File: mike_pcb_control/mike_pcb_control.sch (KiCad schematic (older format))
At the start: 5 parts, among them J1 Conn_01x06_Male, J4 Raspberry_Pi_2_3, U3 LLC-4channel, U4 Adafruit_Feather_Pinout

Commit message: Updating the design files
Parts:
- added C1: C, Capacitor_THT:C_Radial_D8.0mm_H7.0mm_P3.50mm, symbol Device:C
- added J2: Conn_01x06_Male, Connector_PinHeader_2.54mm:PinHeader_1x06_P2.54mm_Vertical, symbol Connector:Conn_01x06_Male
- added J3, J5: Conn_01x03_Male, Connector_PinHeader_2.54mm:PinHeader_1x03_P2.54mm_Vertical, symbol Connector:Conn_01x03_Male
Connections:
- net +5V: now also C1.1, J2.5 (Pin_5), J2.6 (Pin_6), J3.3 (Pin_3), J5.3 (Pin_3)
- net GND: now also C1.2, J2.3 (Pin_3), J2.4 (Pin_4), J3.2 (Pin_2), J5.2 (Pin_2)
- net RX5V: now also J2.1 (Pin_1)
- net SCL3V3: now also U4.18
- net SCL5V: now also A2.24 (A5)
- net SDA3V3: now also U4.17
- net SDA5V: now also A2.23 (A4)
- net TX5V: now also J2.2 (Pin_2)
- net A0: now reaches A2.19 (A0)
- net A0: now also J5.1 (Pin_1)
- net A1: now reaches A2.20 (A1)
- net A1: now also J3.1 (Pin_1)
- removed net SCL_IMU: A2.24 (A5), U4.18
- removed net SDA_IMU: A2.23 (A4), U4.17
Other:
- moved on the sheet: J1, U3

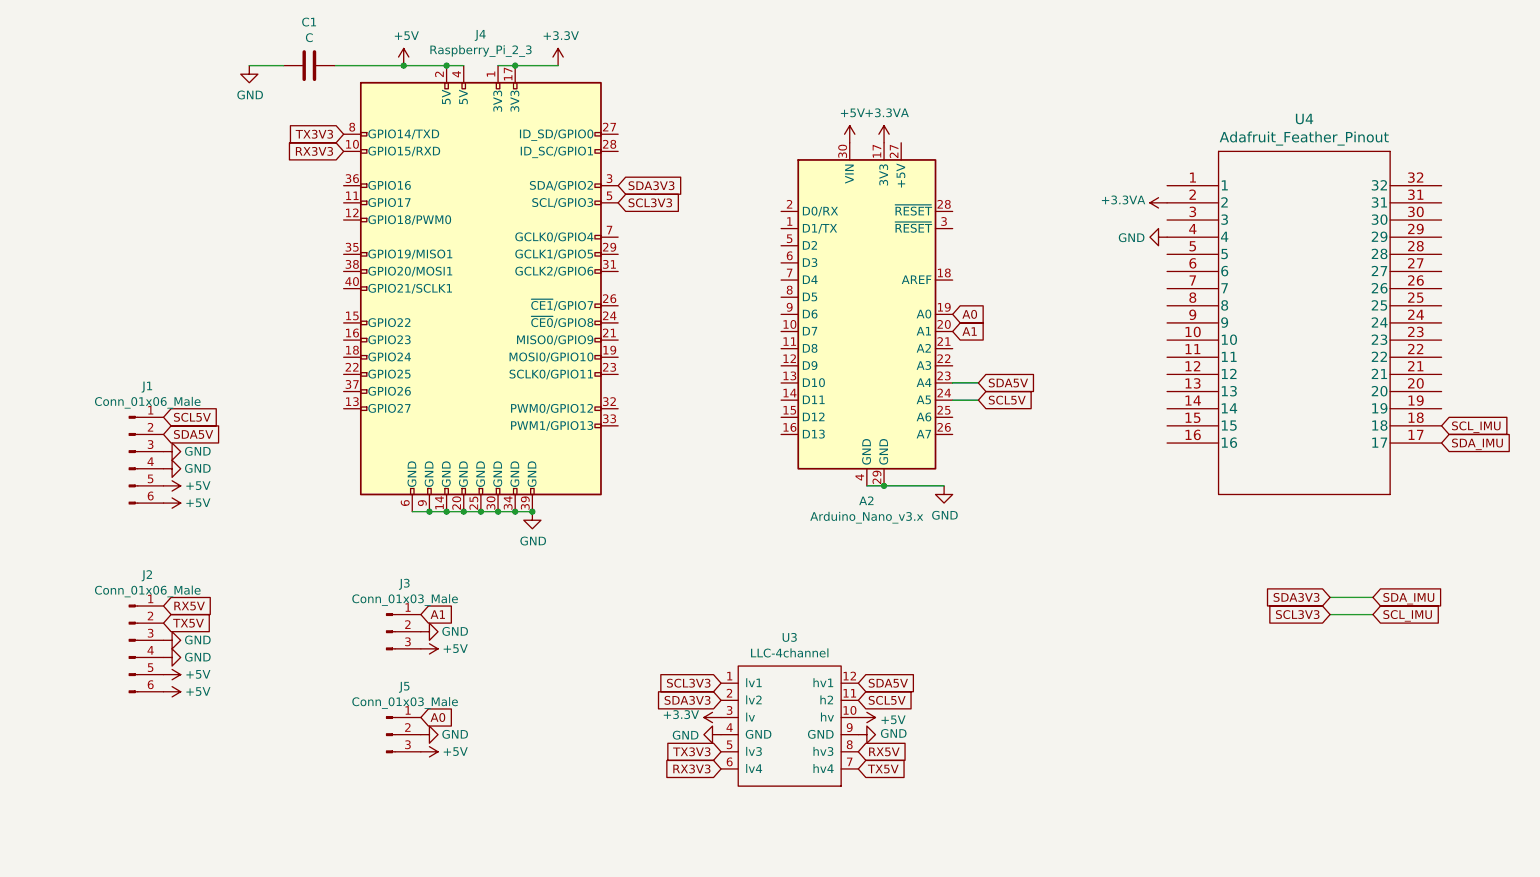
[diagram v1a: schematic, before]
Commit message: PCB bugfix, I2C seperated
I2C for IMU seperated from main I2C bus
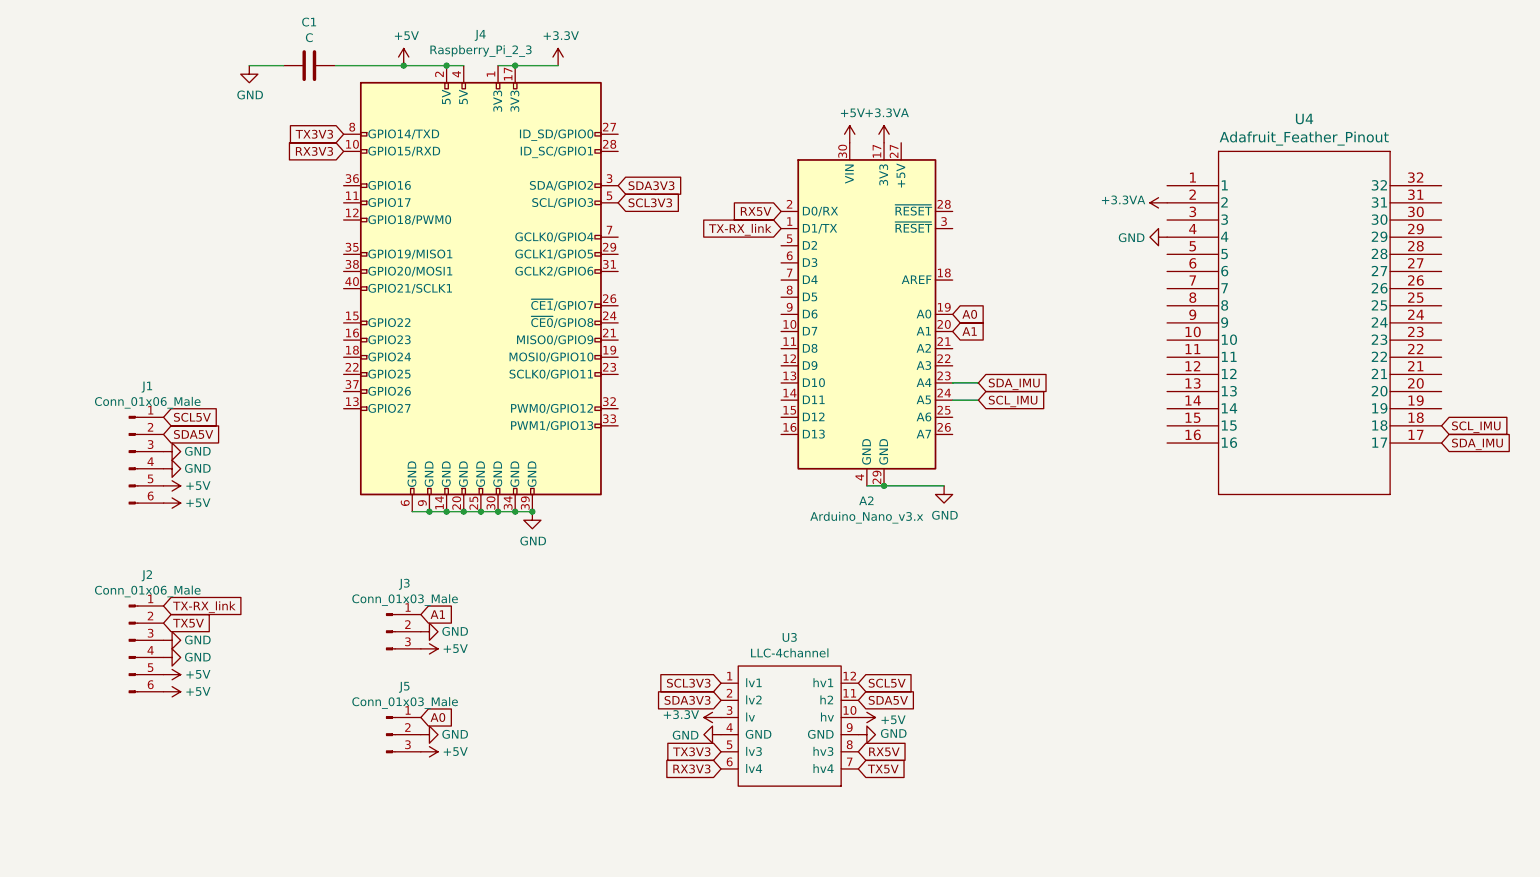
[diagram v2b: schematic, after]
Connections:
- net RX5V: now also A2.2 (D0/RX); no longer J2.1 (Pin_1)
- net SCL3V3: no longer U4.18
- net SCL5V: now also U3.12 (hv1); no longer A2.24 (A5), U3.11 (h2)
- net SDA3V3: no longer U4.17
- net SDA5V: now also U3.11 (h2); no longer A2.23 (A4), U3.12 (hv1)
- net TX-RX_link: now reaches A2.1 (D1/TX)
- net TX-RX_link: now also J2.1 (Pin_1)
- new net SCL_IMU: A2.24 (A5), U4.18
- new net SDA_IMU: A2.23 (A4), U4.17
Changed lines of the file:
@@
 Text GLabel 10100 3400 2    50   Input ~ 0
 SCL_IMU
-Text GLabel 9700 4500 2    50   Input ~ 0
+Text GLabel 7400 3250 2    50   Input ~ 0
 SCL_IMU
-Text GLabel 9700 4400 2    50   Input ~ 0
+Text GLabel 7400 3150 2    50   Input ~ 0
 SDA_IMU
 Text GLabel 5300 2100 2    50   Input ~ 0
@@
 Text GLabel 5900 5000 0    50   Input ~ 0
 SDA3V3
+Text GLabel 6700 4900 2    50   Input ~ 0
+SCL5V
 Text GLabel 6700 5000 2    50   Input ~ 0
-SCL5V
-Text GLabel 6700 4900 2    50   Input ~ 0
 SDA5V
 $Comp
@@
 	0    1    1    0
 $EndComp
-Text GLabel 9450 4500 0    50   Input ~ 0
-SCL3V3
-Text GLabel 9450 4400 0    50   Input ~ 0
-SDA3V3
-Wire Wire Line
-	9450 4400 9700 4400
-Wire Wire Line
-	9700 4500 9450 4500
-Text GLabel 7400 3250 2    50   Input ~ 0
-SCL5V
-Text GLabel 7400 3150 2    50   Input ~ 0
-SDA5V
 Wire Wire Line
 	7400 3150 7250 3150
@@
 	0    1    1    0
 $EndComp
-Text GLabel 2650 4450 2    50   Input ~ 0
+Text GLabel 6250 2150 0    50   Input ~ 0
 RX5V
 Text GLabel 2650 4550 2    50   Input ~ 0
@@
 Wire Wire Line
 	3350 1300 3150 1300
+Text GLabel 6250 2250 0    50   Input ~ 0
+TX-RX_link
+Text GLabel 2650 4450 2    50   Input ~ 0
+TX-RX_link
 $EndSCHEMATC
